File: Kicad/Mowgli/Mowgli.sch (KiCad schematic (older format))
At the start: 1 part

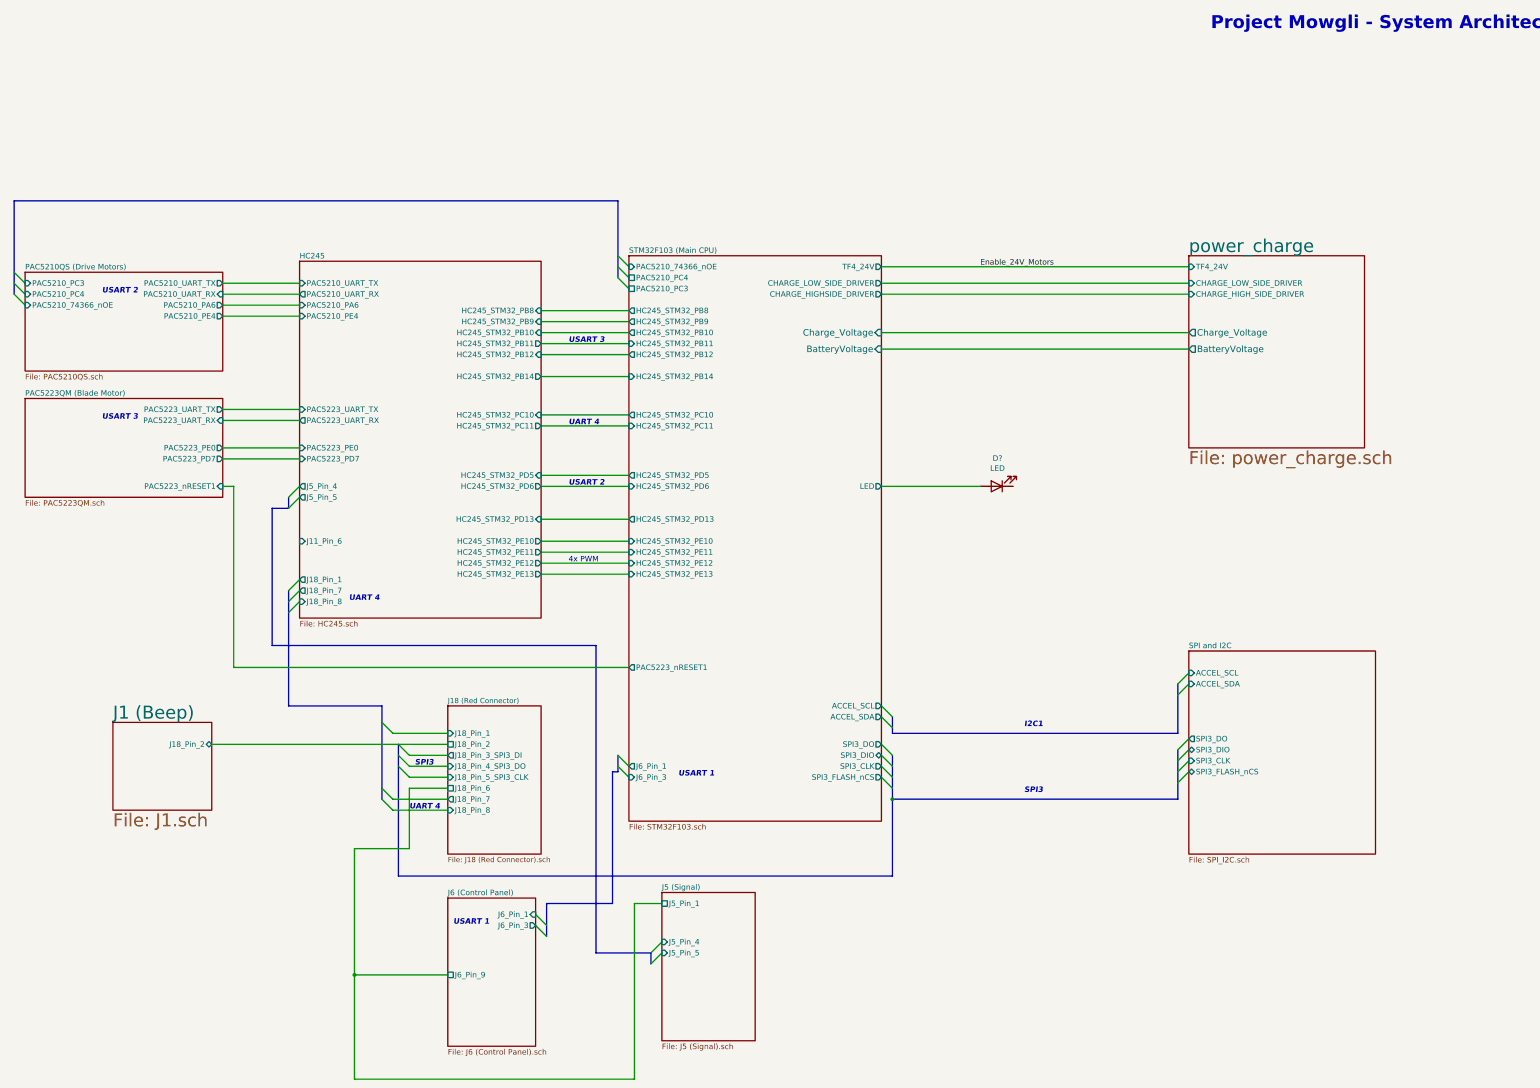
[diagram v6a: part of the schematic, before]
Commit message: added more details to panel J6 connector, and reversed rain sensor (STM32 PE2)
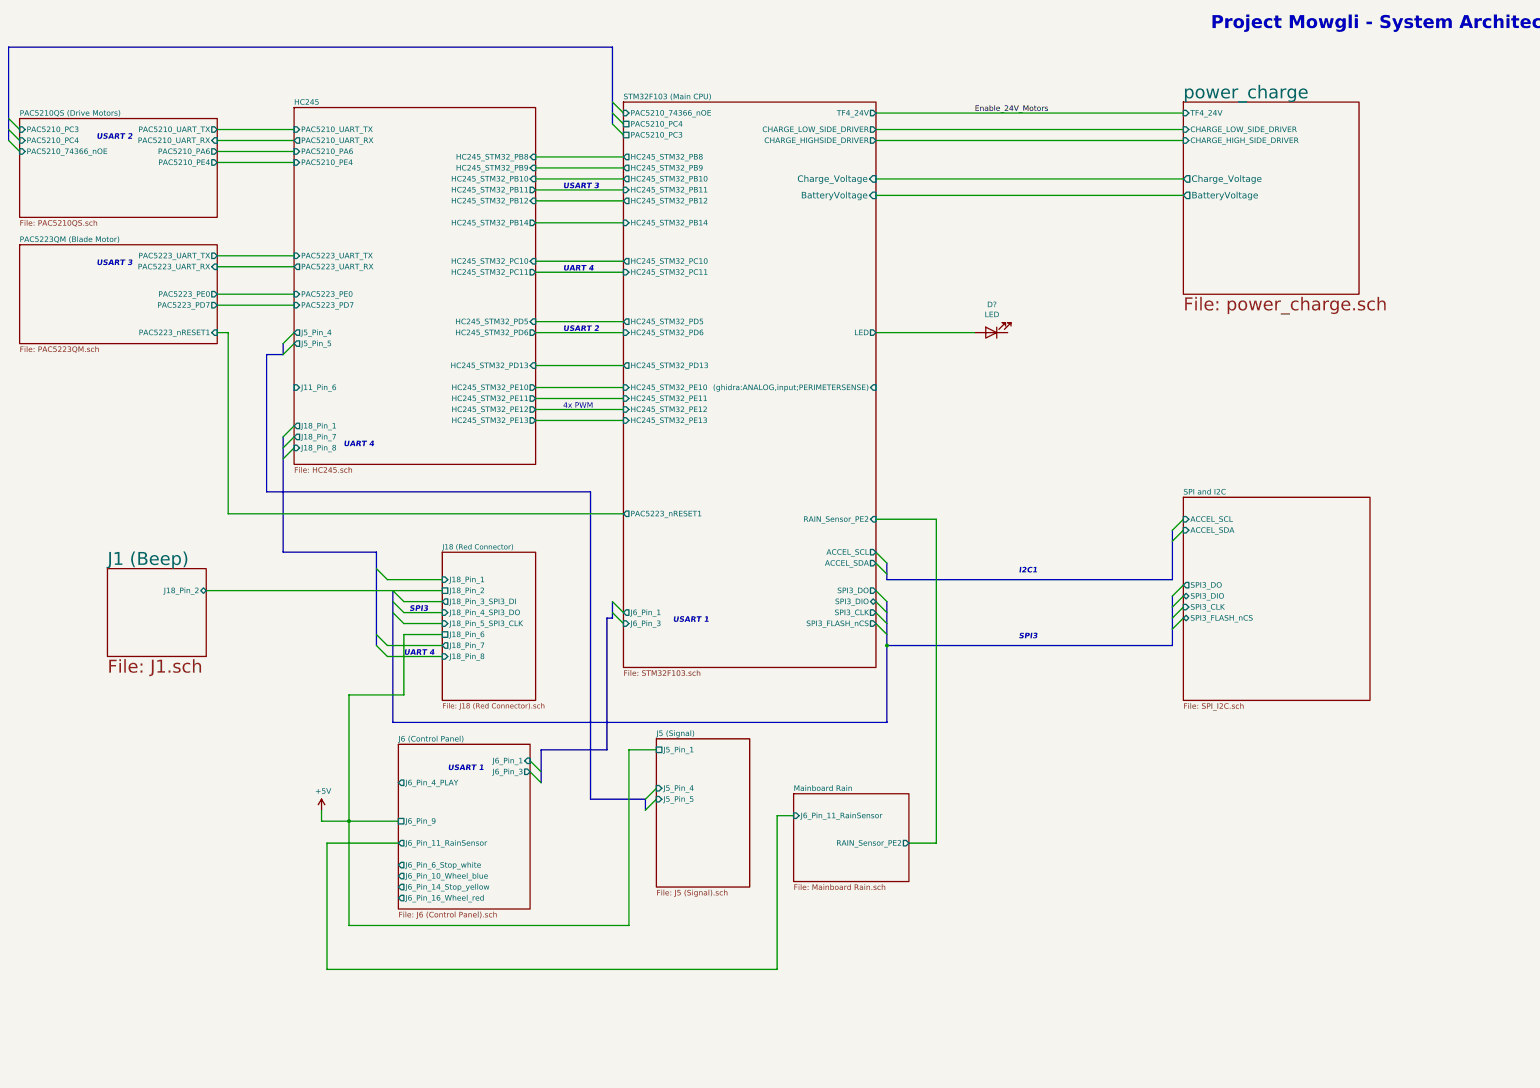
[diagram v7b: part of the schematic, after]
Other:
- moved on the sheet: D?

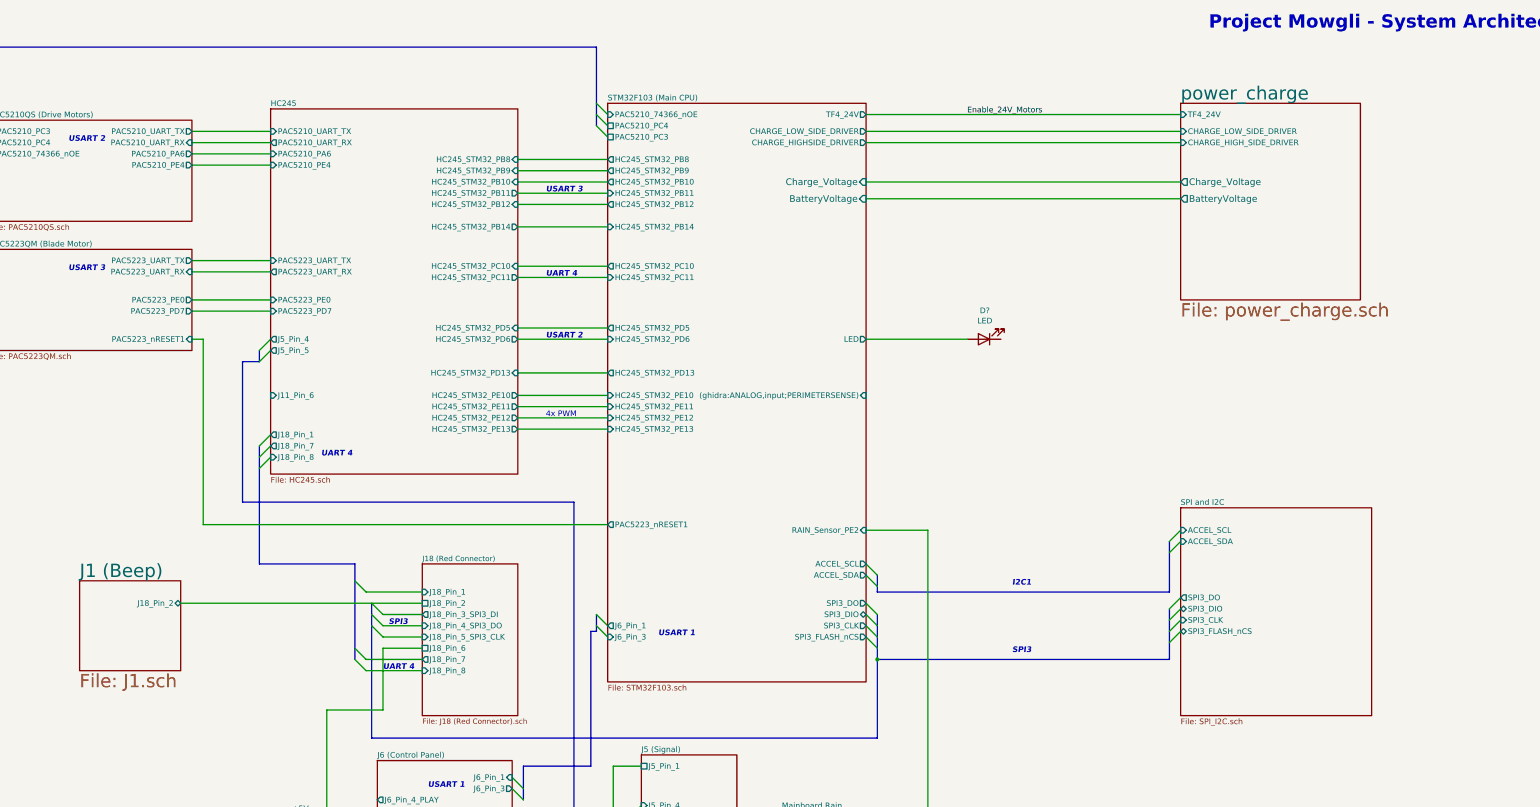
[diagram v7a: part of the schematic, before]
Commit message: added some datasheets, kicad updates
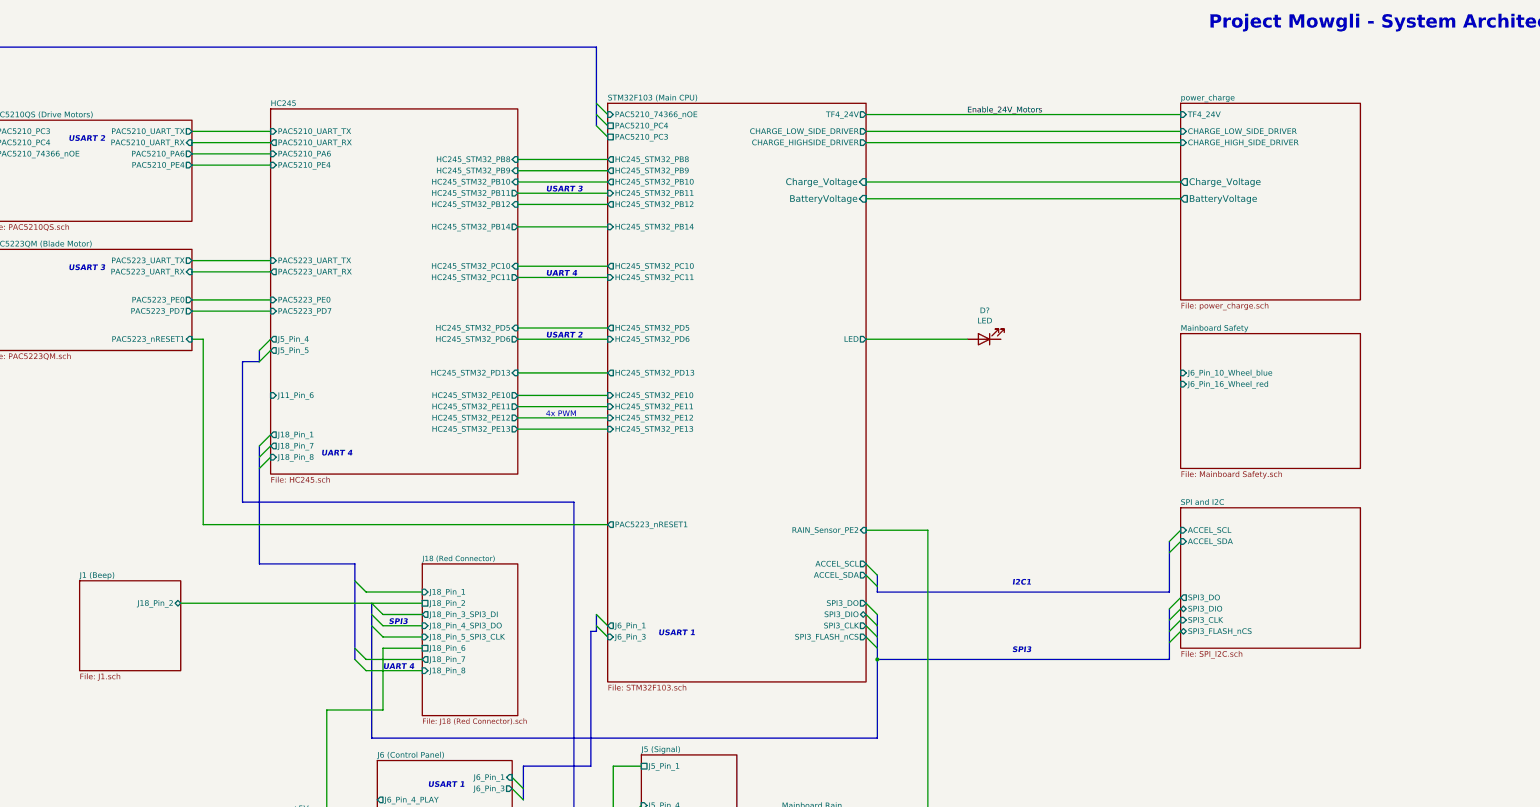
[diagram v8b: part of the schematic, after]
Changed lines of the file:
@@
 $Descr A3 16535 11693
 encoding utf-8
-Sheet 1 12
+Sheet 1 13
 Title "Project Mowgli"
 Date "2022-05-22"
@@
 F33 "Charge_Voltage" I R 9450 2150 59
 F34 "BatteryVoltage" I R 9450 2300 59
-F35 "(ghidra:ANALOG,input;PERIMETERSENSE)" I R 9450 4050 50
-F36 "RAIN_Sensor_PE2" I R 9450 5250 50
+F35 "RAIN_Sensor_PE2" I R 9450 5250 50
 $EndSheet
 Wire Wire Line
@@
 	9450 6200 9550 6300
 $Sheet
-S 12250 5050 1700 1850
+S 12250 5050 1600 1250
 U 6293F03E
 F0 "SPI and I2C" 50
@@
 S 12250 1450 1600 1750
 U 628DB6FB
-F0 "power_charge" 118
-F1 "power_charge.sch" 118
+F0 "power_charge" 50
+F1 "power_charge.sch" 50
 F2 "TF4_24V" I L 12250 1550 50
 F3 "CHARGE_LOW_SIDE_DRIVER" I L 12250 1700 50
@@
 S 2450 5700 900  800
 U 629B383F
-F0 "J1 (Beep)" 118
-F1 "J1.sch" 118
+F0 "J1 (Beep)" 50
+F1 "J1.sch" 50
 F2 "J18_Pin_2" B R 3350 5900 50
 $EndSheet
@@
 Wire Bus Line
 	9550 6000 9550 6400
+$Sheet
+S 12250 3500 1600 1200
+U 62BC248C
+F0 "Mainboard Safety" 50
+F1 "Mainboard Safety.sch" 50
+F2 "J6_Pin_16_Wheel_red" I L 12250 3950 50
+F3 "J6_Pin_10_Wheel_blue" I L 12250 3850 50
+$EndSheet
 $EndSCHEMATC
